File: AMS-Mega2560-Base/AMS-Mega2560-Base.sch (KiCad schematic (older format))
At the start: 18 parts, among them J1 RTD1, J2 RTD2, J3 AdafruitUltimateGPS, J4 Sense, J5 Sense, P1 Power, P10 CONN_01X01, P11 CONN_01X01, P12 CONN_01X01, P13 CONN_01X01, P2 Analog, P3 Analog, P4 Digital, P5 PWM, P6 PWM, P7 Communication, P8 CONN_01X01, P9 CONN_01X01

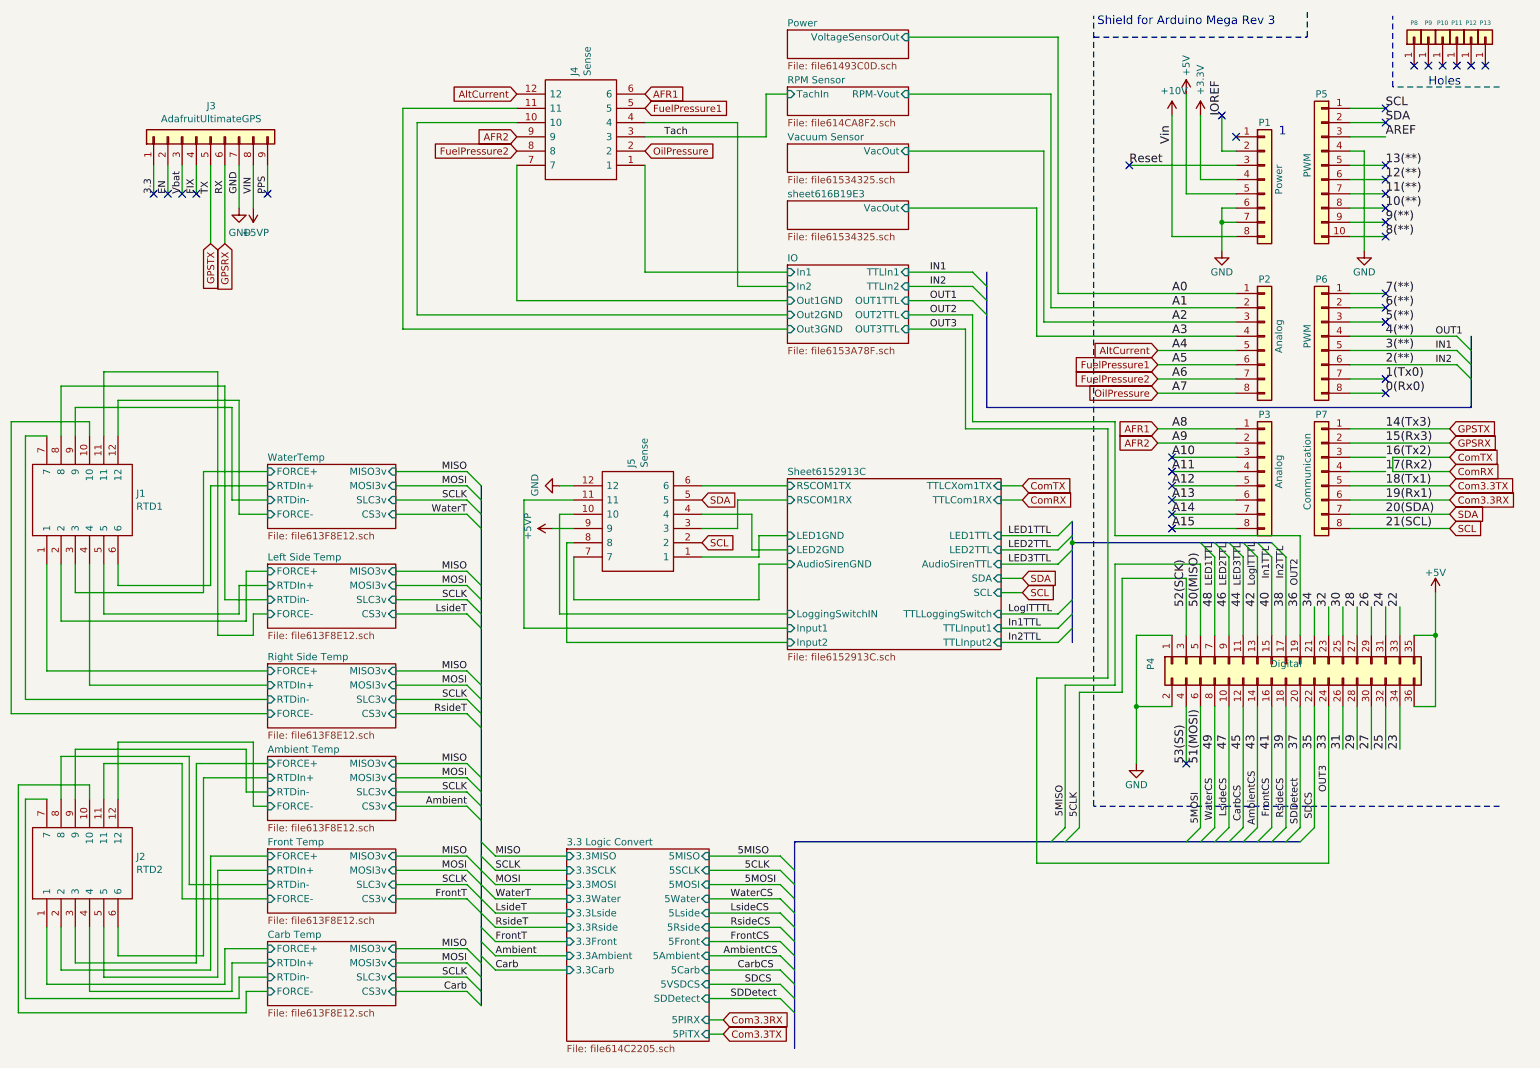
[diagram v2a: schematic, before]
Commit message: upgrading this to 6.0 and moving the vacuum sensors to a daughter board project.
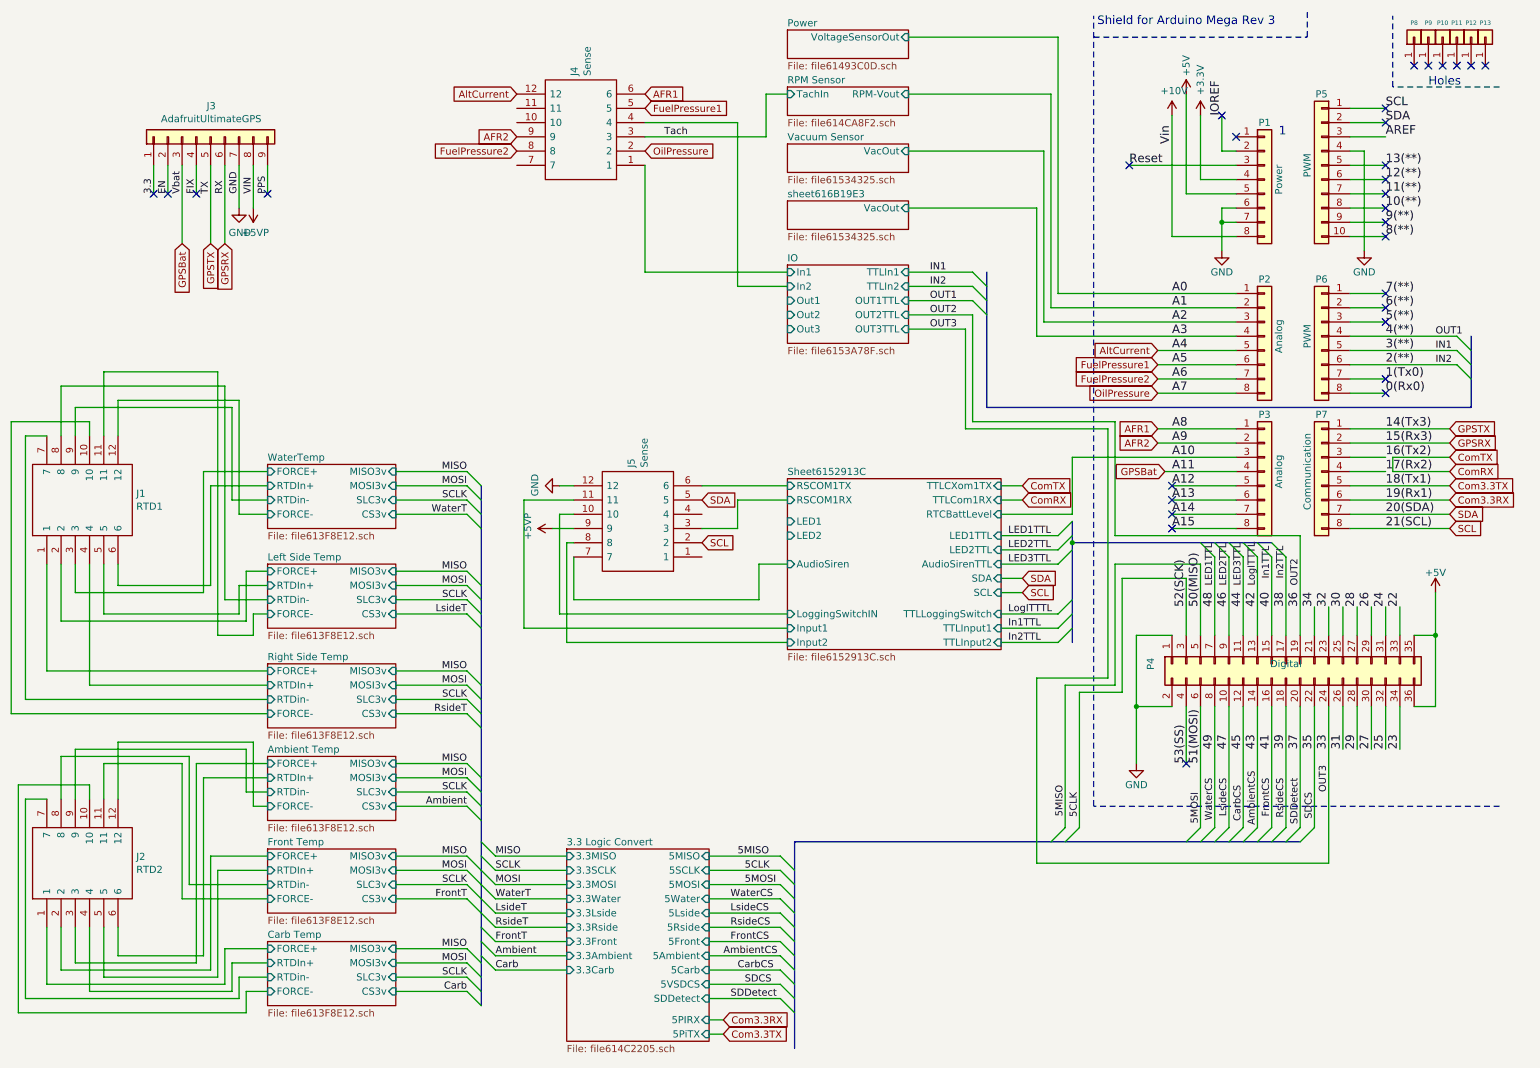
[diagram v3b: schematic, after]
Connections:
- net Vbat is gone; now on net GPSBat: J3.3 (Pin_3)
- net A11 renamed GPSBat
- net IO/Out1GND: no longer names the net of J4.7
- net IO/Out2GND: no longer names the net of J4.10
- net IO/Out3GND: no longer names the net of J4.11
- net Sheet6152913C/AudioSirenGND renamed Sheet6152913C/AudioSiren
- net Sheet6152913C/LED1GND: no longer names the net of J5.1
- net Sheet6152913C/LED2GND: no longer names the net of J5.4
- no-connect marks 34 -> 31
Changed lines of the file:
@@
 	10150 3150 10400 3150
-Wire Wire Line
-	9350 3600 8900 3600
-Wire Wire Line
-	8900 3700 9350 3700
 Wire Wire Line
 	9350 3800 8900 3800
@@
 	2050 1750 2050 1550
 Wire Wire Line
-	1950 1750 1950 1550
-Wire Wire Line
 	1850 1750 1850 1550
 Wire Wire Line
@@
 NoConn ~ 1750 1750
 NoConn ~ 1850 1750
-NoConn ~ 1950 1750
 NoConn ~ 2050 1750
 NoConn ~ 2550 1750
@@
 F0 "IO" 50
 F1 "file6153A78F.sch" 50
-F2 "Out3GND" I L 6200 2700 50
-F3 "OUT3TTL" I R 7050 2700 50
-F4 "Out2GND" I L 6200 2600 50
-F5 "OUT2TTL" I R 7050 2600 50
-F6 "In2" I L 6200 2400 50
-F7 "TTLIn2" I R 7050 2400 50
-F8 "Out1GND" I L 6200 2500 50
-F9 "OUT1TTL" I R 7050 2500 50
-F10 "In1" I L 6200 2300 50
-F11 "TTLIn1" I R 7050 2300 50
+F2 "OUT3TTL" I R 7050 2700 50
+F3 "OUT2TTL" I R 7050 2600 50
+F4 "In2" I L 6200 2400 50
+F5 "TTLIn2" I R 7050 2400 50
+F6 "OUT1TTL" I R 7050 2500 50
+F7 "In1" I L 6200 2300 50
+F8 "TTLIn1" I R 7050 2300 50
+F9 "Out3" I L 6200 2700 50
+F10 "Out2" I L 6200 2600 50
+F11 "Out1" I L 6200 2500 50
 $EndSheet
 Text GLabel 5600 4200 2    50   Input ~ 0
@@
 NoConn ~ 8900 3900
 NoConn ~ 8900 3800
-NoConn ~ 8900 3700
-NoConn ~ 8900 3600
 Wire Wire Line
 	5600 4100 5850 4100
@@
 $EndComp
 Wire Wire Line
-	5600 4300 6000 4300
-Wire Wire Line
-	6000 4300 6000 4150
-Wire Wire Line
-	6000 4150 6200 4150
-Wire Wire Line
-	6200 4250 5950 4250
-Wire Wire Line
-	5950 4250 5950 4000
-Wire Wire Line
-	5950 4000 5600 4000
-Wire Wire Line
 	6200 4350 6000 4350
 Wire Wire Line
@@
 Wire Wire Line
 	5850 1250 5200 1250
-Wire Wire Line
-	6200 2500 4300 2500
-Wire Wire Line
-	4300 2500 4300 1550
-Wire Wire Line
-	6200 2600 3600 2600
-Wire Wire Line
-	3600 2600 3600 1250
-Wire Wire Line
-	3600 1250 4300 1250
-Wire Wire Line
-	6200 2700 3500 2700
-Wire Wire Line
-	3500 2700 3500 1150
-Wire Wire Line
-	3500 1150 4300 1150
 Wire Bus Line
 	11000 3250 7600 3250
@@
 F2 "RSCOM1TX" I L 6200 3800 50
 F3 "RSCOM1RX" I L 6200 3900 50
-F4 "LED1GND" I L 6200 4150 50
-F5 "LED2GND" I L 6200 4250 50
-F6 "Input2" I L 6200 4900 50
-F7 "Input1" I L 6200 4800 50
-F8 "AudioSirenGND" I L 6200 4350 50
-F9 "TTLCXom1TX" I R 7700 3800 50
-F10 "TTLCom1RX" I R 7700 3900 50
-F11 "LED1TTL" I R 7700 4150 50
-F12 "LED2TTL" I R 7700 4250 50
-F13 "AudioSirenTTL" I R 7700 4350 50
-F14 "SDA" I R 7700 4450 50
-F15 "SCL" I R 7700 4550 50
-F16 "TTLLoggingSwitch" I R 7700 4700 50
-F17 "TTLInput1" I R 7700 4800 50
-F18 "TTLInput2" I R 7700 4900 50
-F19 "LoggingSwitchIN" I L 6200 4700 50
+F4 "Input2" I L 6200 4900 50
+F5 "Input1" I L 6200 4800 50
+F6 "TTLCXom1TX" I R 7700 3800 50
+F7 "TTLCom1RX" I R 7700 3900 50
+F8 "LED1TTL" I R 7700 4150 50
+F9 "LED2TTL" I R 7700 4250 50
+F10 "AudioSirenTTL" I R 7700 4350 50
+F11 "SDA" I R 7700 4450 50
+F12 "SCL" I R 7700 4550 50
+F13 "TTLLoggingSwitch" I R 7700 4700 50
+F14 "TTLInput1" I R 7700 4800 50
+F15 "TTLInput2" I R 7700 4900 50
+F16 "LoggingSwitchIN" I L 6200 4700 50
+F17 "RTCBattLevel" I R 7700 4000 50
+F18 "LED1" I L 6200 4050 50
+F19 "LED2" I L 6200 4150 50
+F20 "AudioSiren" I L 6200 4350 50
 $EndSheet
 Wire Wire Line
@@
 Wire Wire Line
 	5650 7650 5750 7650
+Wire Wire Line
+	7700 4000 8200 4000
+Wire Wire Line
+	8200 4000 8200 3600
+Wire Wire Line
+	8200 3600 9350 3600
+Text GLabel 8850 3700 0    50   Input ~ 0
+GPSBat
+Wire Wire Line
+	8850 3700 9350 3700
+Text GLabel 1950 2100 3    50   Input ~ 0
+GPSBat
+Wire Wire Line
+	1950 1550 1950 2100
 Wire Bus Line
 	8200 4050 8200 4200
